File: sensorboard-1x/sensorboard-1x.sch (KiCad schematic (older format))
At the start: 8 parts, among them J1 Conn_02x02_Odd_Even, U1 CNY70

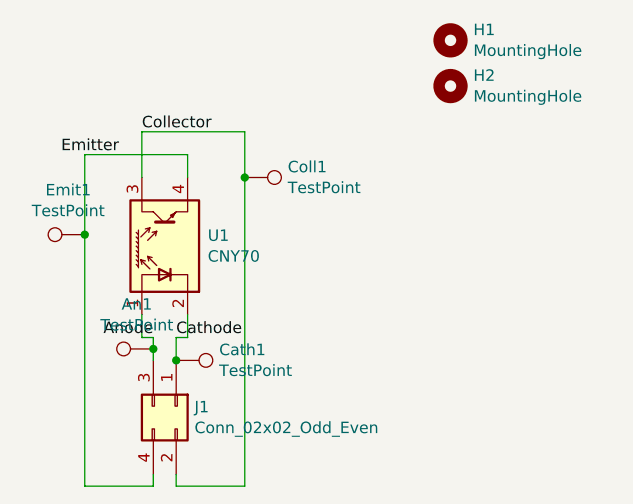
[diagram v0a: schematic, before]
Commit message: shrunk the sensorboard slightly, removed extra mounting hole.
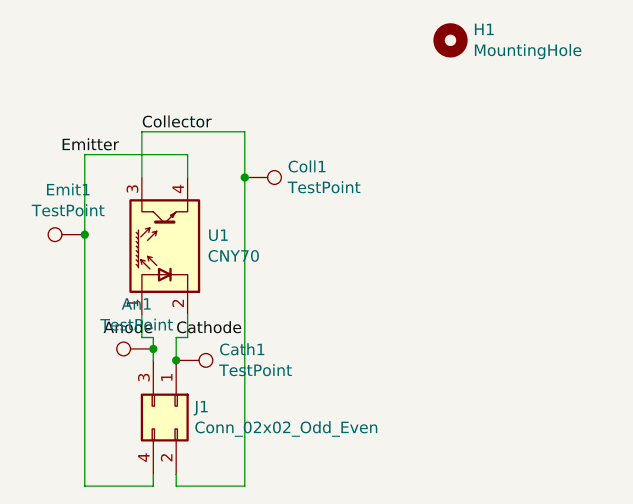
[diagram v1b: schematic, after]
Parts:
- removed H2: MountingHole, Mounting_Holes:MountingHole_3.2mm_M3, symbol Mechanical:MountingHole
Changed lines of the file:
@@
-	1    0    0    -1
-$EndComp
-$Comp
-L Mechanical:MountingHole H2
-U 1 1 5F9EDDDA
-P 7000 2400
-F 0 "H2" H 7100 2446 50  0000 L CNN
-F 1 "MountingHole" H 7100 2355 50  0000 L CNN
-F 2 "Mounting_Holes:MountingHole_3.2mm_M3" H 7000 2400 50  0001 C CNN
-F 3 "~" H 7000 2400 50  0001 C CNN
-	1    7000 2400
 	1    0    0    -1
 $EndComp

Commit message: Narrowed the board, better matching Cybrid's dimensions.
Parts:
- An1, Cath1: footprint TestPoint:TestPoint_Pad_D1.0mm -> TestPoint:TestPoint_Pad_1.5x1.5mm
- Coll1, Emit1: footprint TestPoint:TestPoint_Pad_D1.0mm -> TestPoint:TestPoint_Pad_D1.5mm
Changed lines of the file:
@@
 F 0 "Coll1" V 6054 2988 50  0000 L CNN
 F 1 "TestPoint" V 6145 2988 50  0000 L CNN
-F 2 "TestPoint:TestPoint_Pad_D1.0mm" H 6300 2800 50  0001 C CNN
+F 2 "TestPoint:TestPoint_Pad_D1.5mm" H 6300 2800 50  0001 C CNN
 F 3 "~" H 6300 2800 50  0001 C CNN
 	1    6100 2800
@@
 F 0 "Emit1" V 5595 3122 50  0000 C CNN
 F 1 "TestPoint" V 5504 3122 50  0000 C CNN
-F 2 "TestPoint:TestPoint_Pad_D1.0mm" H 5600 3050 50  0001 C CNN
+F 2 "TestPoint:TestPoint_Pad_D1.5mm" H 5600 3050 50  0001 C CNN
 F 3 "~" H 5600 3050 50  0001 C CNN
 	1    5400 3050
@@
 F 0 "Cath1" V 5754 3788 50  0000 L CNN
 F 1 "TestPoint" V 5845 3788 50  0000 L CNN
-F 2 "TestPoint:TestPoint_Pad_D1.0mm" H 6000 3600 50  0001 C CNN
+F 2 "TestPoint:TestPoint_Pad_1.5x1.5mm" H 6000 3600 50  0001 C CNN
 F 3 "~" H 6000 3600 50  0001 C CNN
 	1    5800 3600
@@
 F 0 "An1" V 5895 3622 50  0000 C CNN
 F 1 "TestPoint" V 5804 3622 50  0000 C CNN
-F 2 "TestPoint:TestPoint_Pad_D1.0mm" H 5900 3550 50  0001 C CNN
+F 2 "TestPoint:TestPoint_Pad_1.5x1.5mm" H 5900 3550 50  0001 C CNN
 F 3 "~" H 5900 3550 50  0001 C CNN
 	1    5700 3550
